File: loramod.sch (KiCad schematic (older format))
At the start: 40 parts

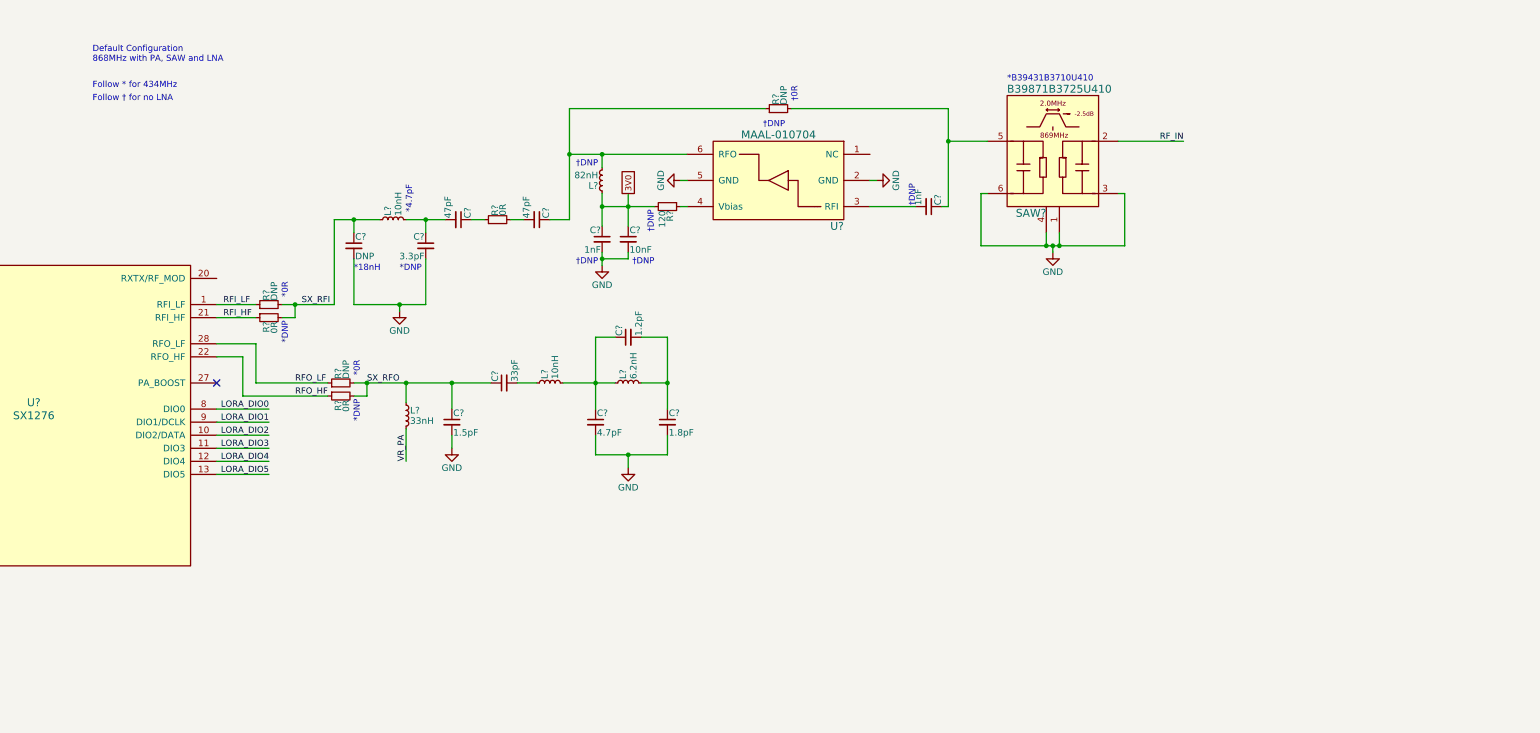
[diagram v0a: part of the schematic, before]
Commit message: Add PA in Tx path
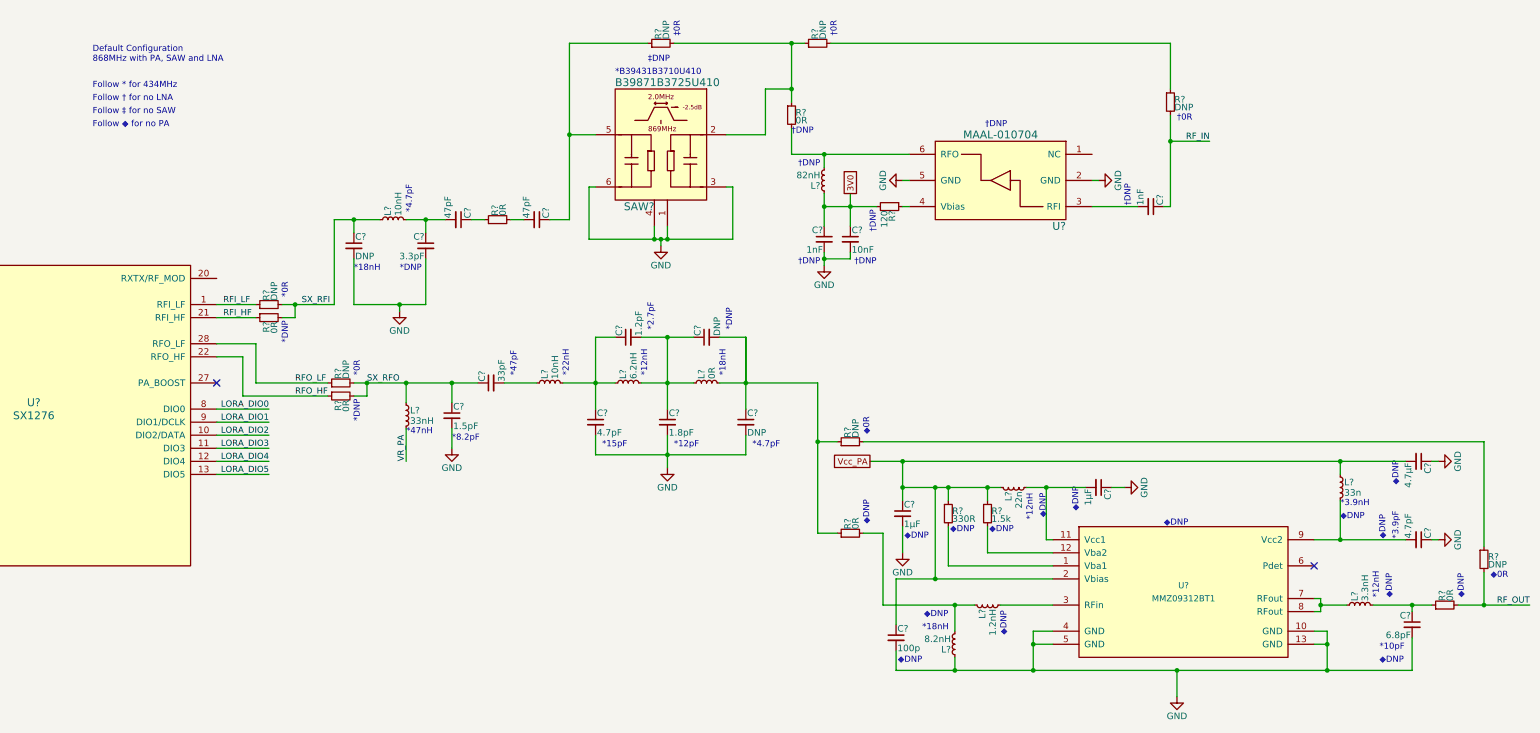
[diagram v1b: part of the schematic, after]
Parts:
- added C? (x2): DNP, symbol C_Small
- added C? (x2): 1µF, symbol C_Small
- added C?: 100p, symbol C_Small
- added C?: 4.7µF, symbol C_Small
- added C?: 4.7pF, symbol C_Small
- added C?: 6.8pF, symbol C_Small
- added L?: 0R, symbol L_Small
- added L?: 1.2nH, symbol L_Small
- added L?: 8.2nH, symbol L_Small
- added L?: 22n, symbol L_Small
- added L?: 33n, symbol L_Small
- added L?: 3.3nH, symbol L_Small
- added R? (x4): DNP, symbol R_Small
- added R? (x3): 0R, symbol R_Small
- added R?: 330R, symbol R_Small
- added R?: 1.5k, symbol R_Small
- added U?: MMZ09312BT1, symbol MMZ09312BT1
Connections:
- net GND: now also C?.1, C?.1, C?.1, C?.2, C?.2, C?.2, C?.2, L?.1, U?.10 (GND), U?.13 (GND), U?.4 (GND), U?.5 (GND)
- net RF_IN: now also C?.1, R?.2; no longer SAW?.2 (IN)
- net at L?.2, U?.6 (RFO): now also R?.2; no longer C?.1, R?.1
- net at C?.1, C?.2, L?.2: now also C?.1, L?.1
- new net: C?.1, R?.1, SAW?.5 (OUT)
- new net: R?.1, R?.1, R?.2, SAW?.2 (IN)
- new net: R?.1, R?.2 (x2)
- new net: C?.1, C?.2, L?.2, R?.1, R?.1
- new net: R?.2, U?.1 (Vba1)
- new net: C?.2, L?.2, U?.11 (Vcc1)
- new net: R?.2, U?.12 (Vba2)
- new net: L?.2, U?.3 (RFin)
- new net: L?.1, U?.7 (RFout), U?.8 (RFout)
- new net: C?.2, L?.2, U?.9 (Vcc2)
- new net: L?.1, L?.2, R?.2
- new net: C?.1, L?.2, R?.1
- new net RF_OUT: R?.2, R?.2
- new net Vcc_PA: C?.1, C?.1, C?.2, L?.1, L?.1, R?.1, R?.1, U?.2 (Vbias)
- no-connect marks 2 -> 3
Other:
- note added: "*10pF"
- note added: "*12nH"
- note added: "*12pF"
- note added: "*15pF"
- note added: "*2.7pF"
- note added: "*22nH"
- note added: "*3.9nH"
- note added: "*3.9pF"
- note added: "*47nH"
- note added: "*47pF"
- note added: "*8.2pF"
- note added: "Follow ‡ for no SAW"
- note added: "Follow ◆ for no PA"
- note added: "‡0R"
- note added: "‡DNP"
- note added: "◆0R"
- note added: "◆DNP"
- moved on the sheet: C?, L?, R?, SAW?, U?

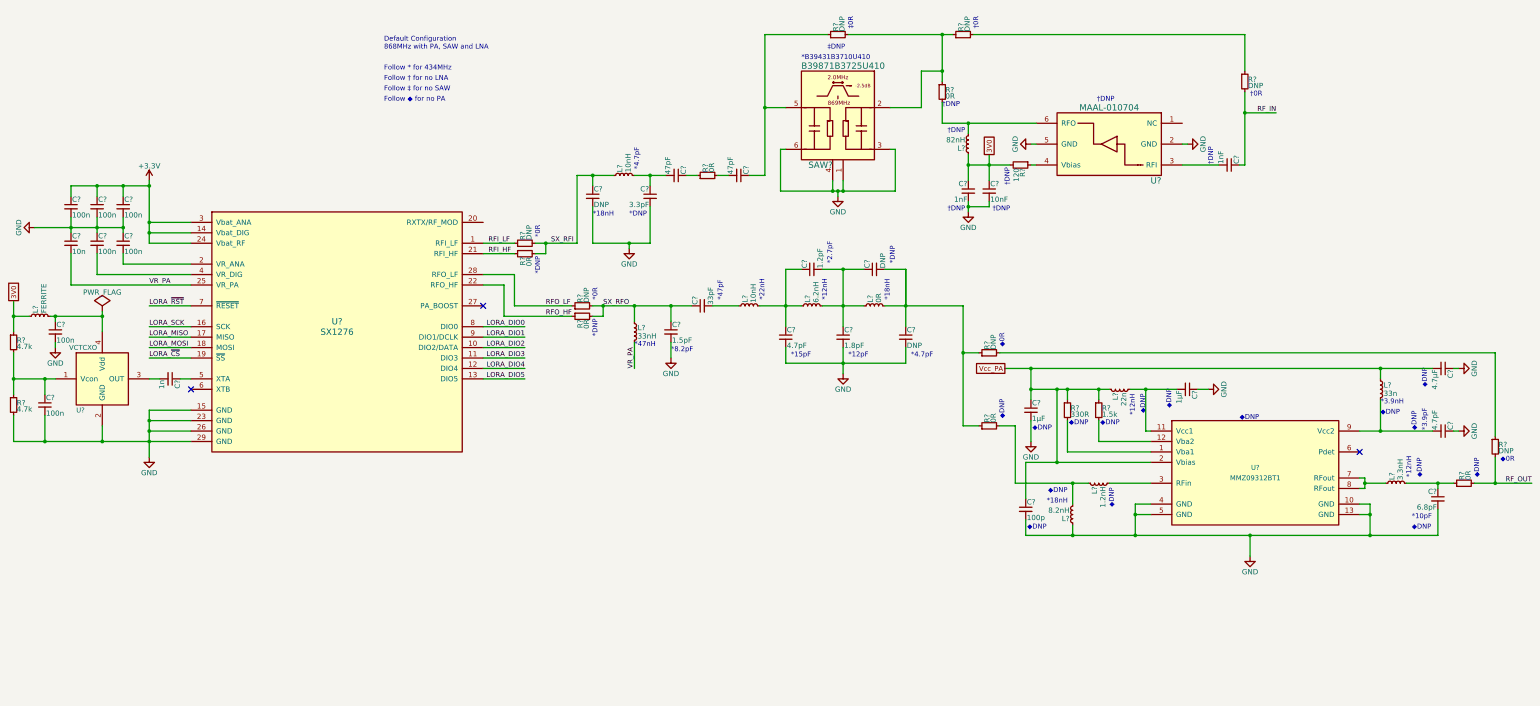
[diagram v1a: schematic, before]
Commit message: Add RF switch
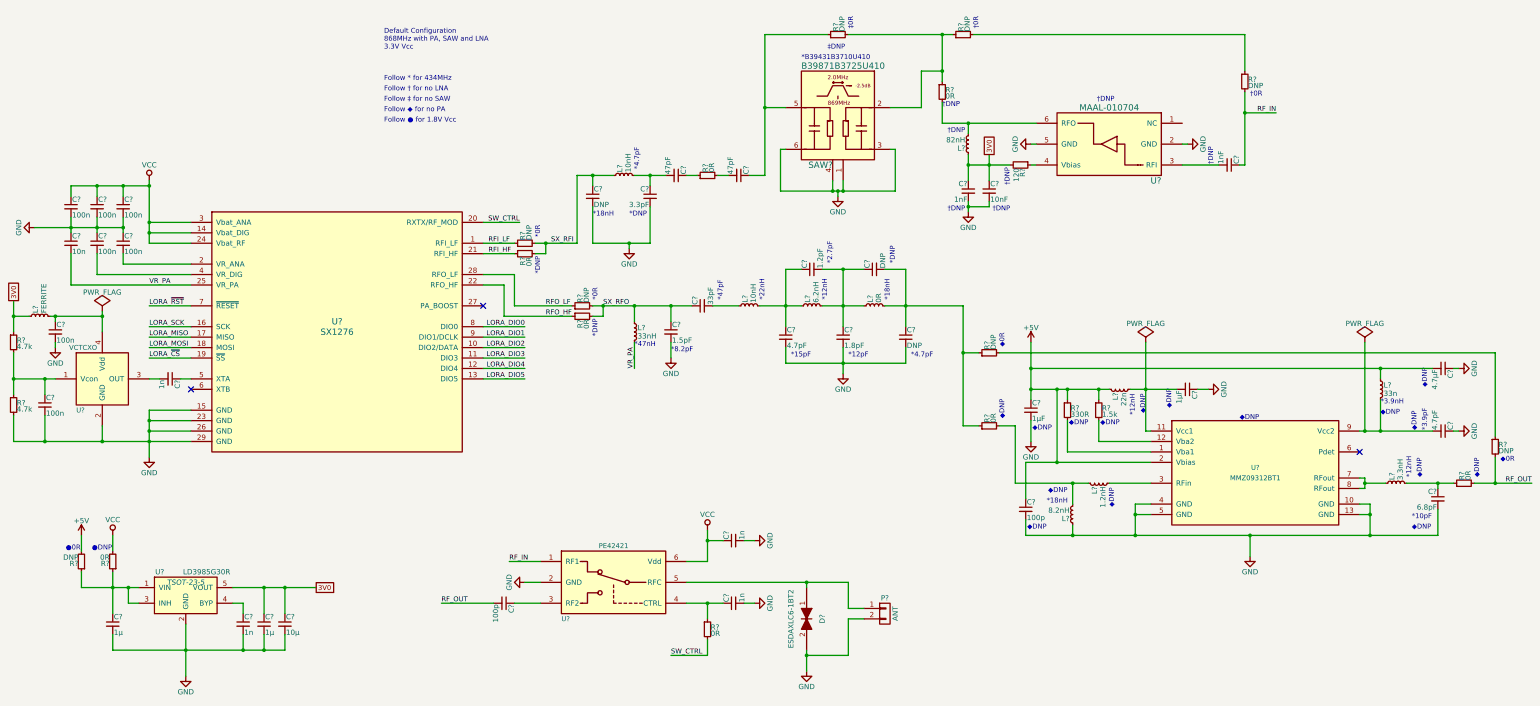
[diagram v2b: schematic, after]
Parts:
- added C? (x3): 1n, symbol C_Small
- added C?: 100p, symbol C_Small
- added C? (x2): 1µ, symbol C_Small
- added C?: 10µ, symbol C_Small
- added D?: ESDAXLC6-1BT2, symbol TVS
- added P?: ANT, symbol CONN_01X02
- added R? (x2): 0R, symbol R_Small
- added R?: DNP, symbol R_Small
- added U?: PE42421, symbol PE42421
- added U?: LD3985G30R, TSOT-23-5, symbol LD3985G30R
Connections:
- net 3V0: now also C?.1, C?.1, U?.5 (VOUT)
- net GND: now also C?.2, C?.2, C?.2, C?.2, C?.2, C?.2, D?.2, P?.2 (P2), U?.2 (GND), U?.2 (GND)
- net RF_IN: now also U?.1 (RF1)
- net RF_OUT: now also C?.2
- net SW_CTRL: now reaches U?.20 (RXTX/RF_MOD)
- net SW_CTRL: now also R?.2
- net +3V3 renamed VCC
- net VCC: now also C?.1, R?.2, U?.6 (Vdd)
- net Vcc_PA renamed +5V
- net +5V: now also R?.2
- new net: C?.1, U?.3 (RF2)
- new net: C?.1, R?.1, U?.4 (CTRL)
- new net: D?.1, P?.1 (P1), U?.5 (RFC)
- new net: C?.1, R?.1, R?.1, U?.1 (VIN), U?.3 (INH)
- new net: C?.1, U?.4 (BYP)
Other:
- note added: "Default Configuration\n868MHz with PA, SAW and LNA\n3.3V Vcc"
- note added: "Follow ● for 1.8V Vcc"
- note added: "●0R"
- note added: "●DNP"
- note removed: "Default Configuration\n868MHz with PA, SAW and LNA"

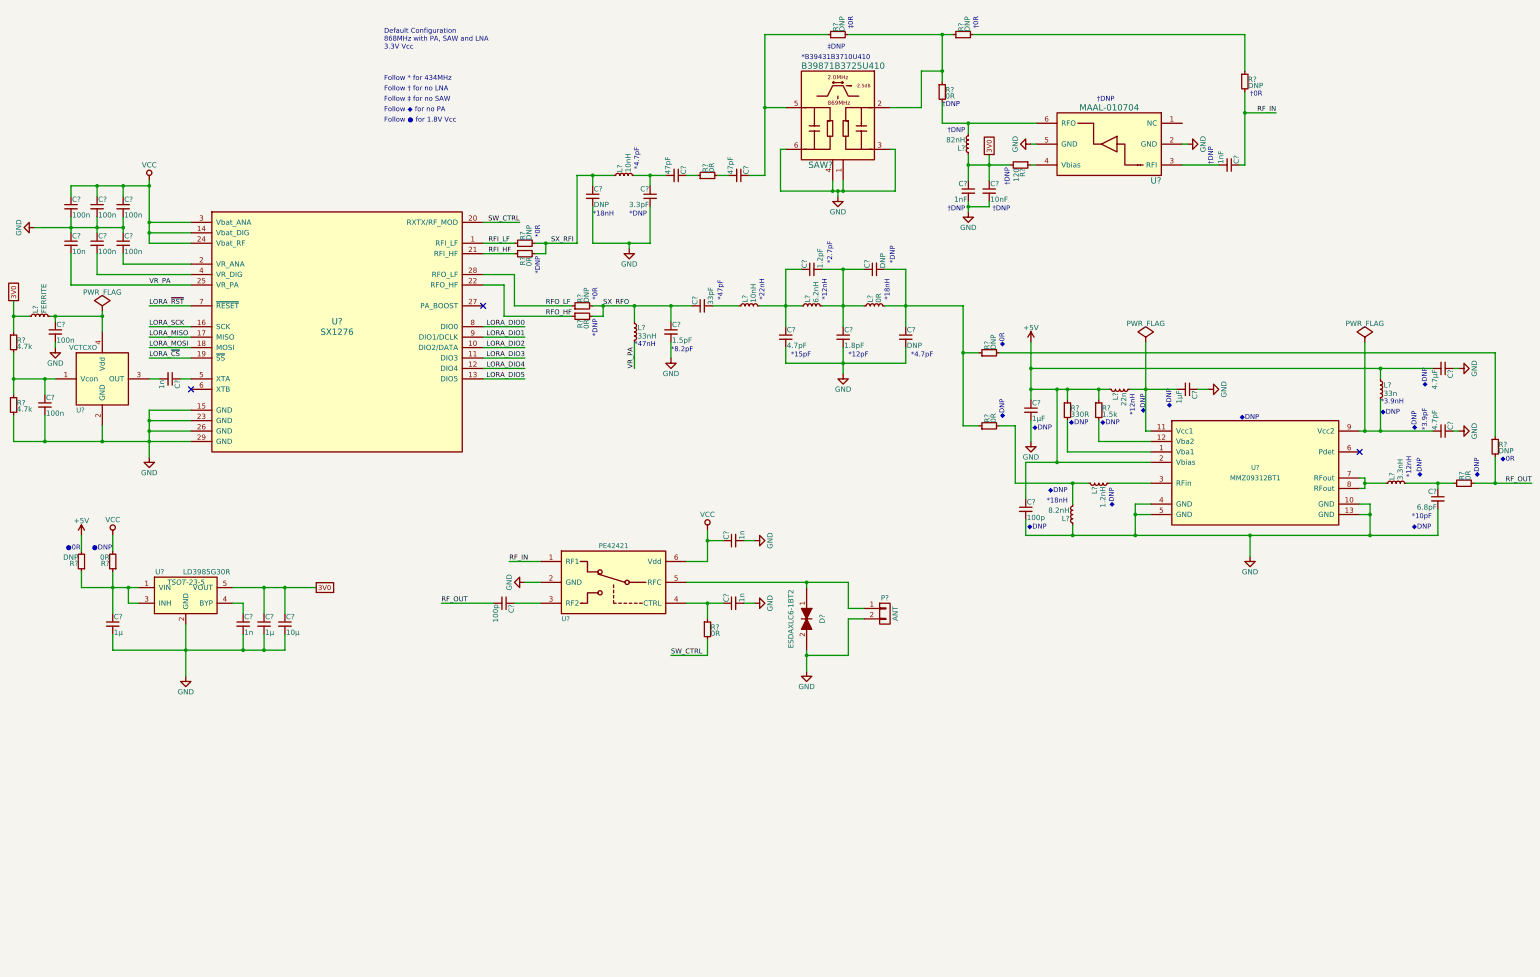
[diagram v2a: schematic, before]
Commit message: Add IO connector; annotate schematic
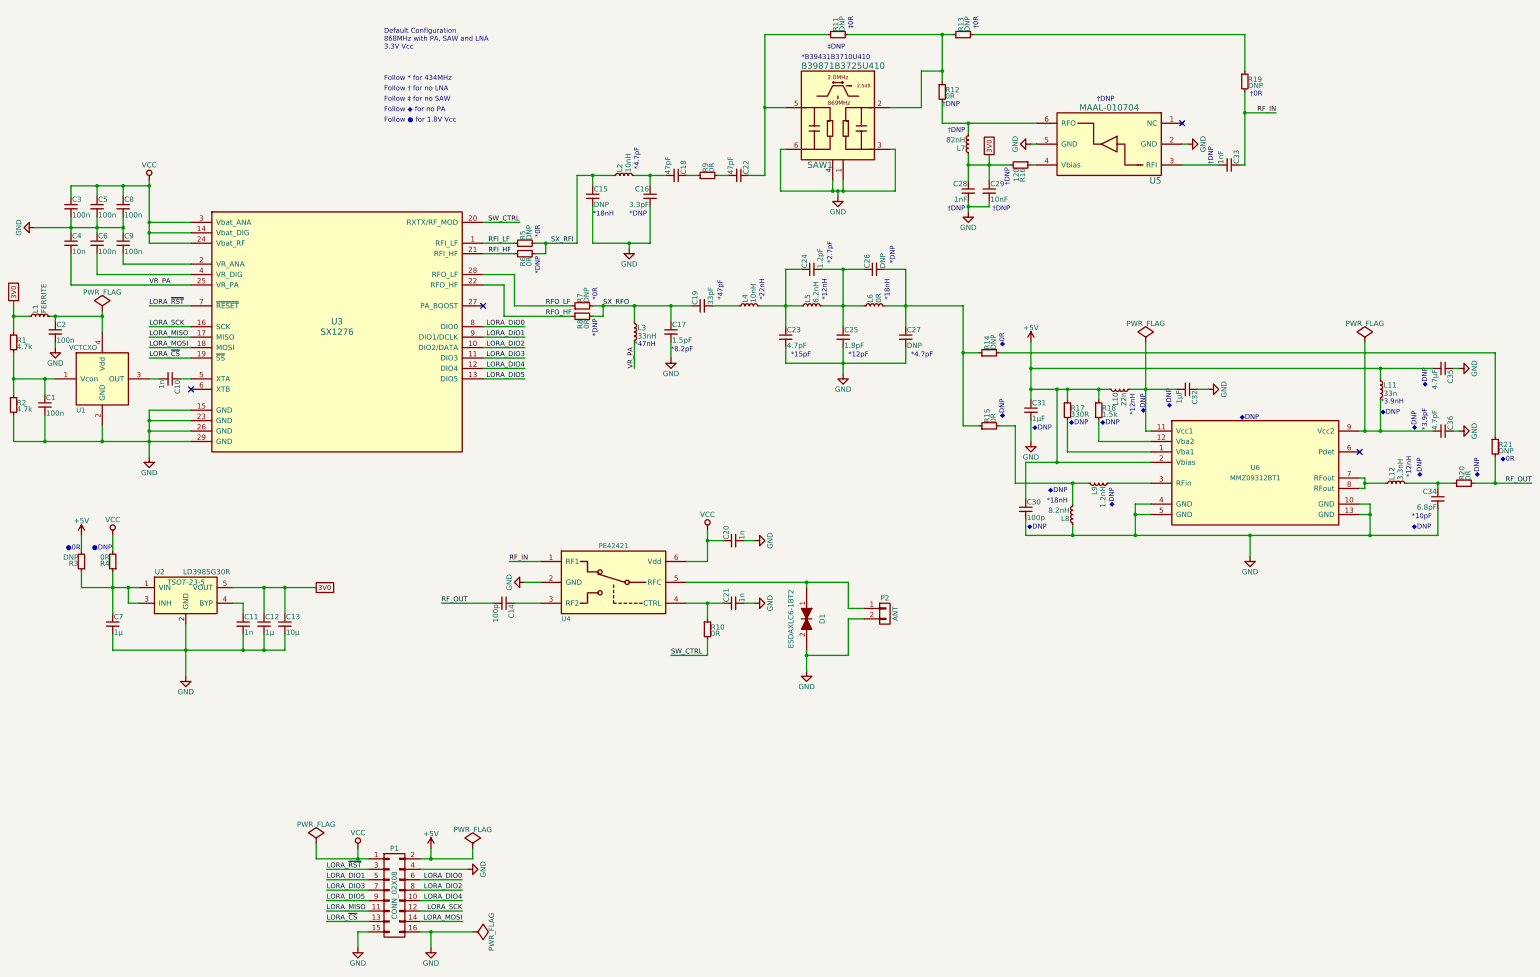
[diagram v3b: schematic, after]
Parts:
- added P1: CONN_02X08, symbol CONN_02X08
- gave numbers to parts that had none: 78
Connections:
- net +5V: now also P1.2 (P2)
- net GND: now also P1.15 (P15), P1.16 (P16), P1.4 (P4)
- net LORA_DIO0: now also P1.6 (P6)
- net LORA_DIO1: now also P1.5 (P5)
- net LORA_DIO2: now also P1.8 (P8)
- net LORA_DIO3: now also P1.7 (P7)
- net LORA_DIO4: now also P1.10 (P10)
- net LORA_DIO5: now also P1.9 (P9)
- net LORA_MISO: now also P1.11 (P11)
- net LORA_MOSI: now also P1.14 (P14)
- net LORA_SCK: now also P1.12 (P12)
- net LORA_~CS: now also P1.13 (P13)
- net LORA_~RST: now also P1.3 (P3)
- net VCC: now also P1.1 (P1)
- no-connect marks 3 -> 4
